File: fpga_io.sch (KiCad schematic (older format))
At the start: 27 parts, among them P1 CONN_5X2, P10 CONN_5X2, P11 CONN_5X2, P12 CONN_5X2, P13 CONN_5X2, P14 CONN_5X2, P2 CONN_5X2, P3 CONN_5X2, P4 CONN_5X2, P5 CONN_5X2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

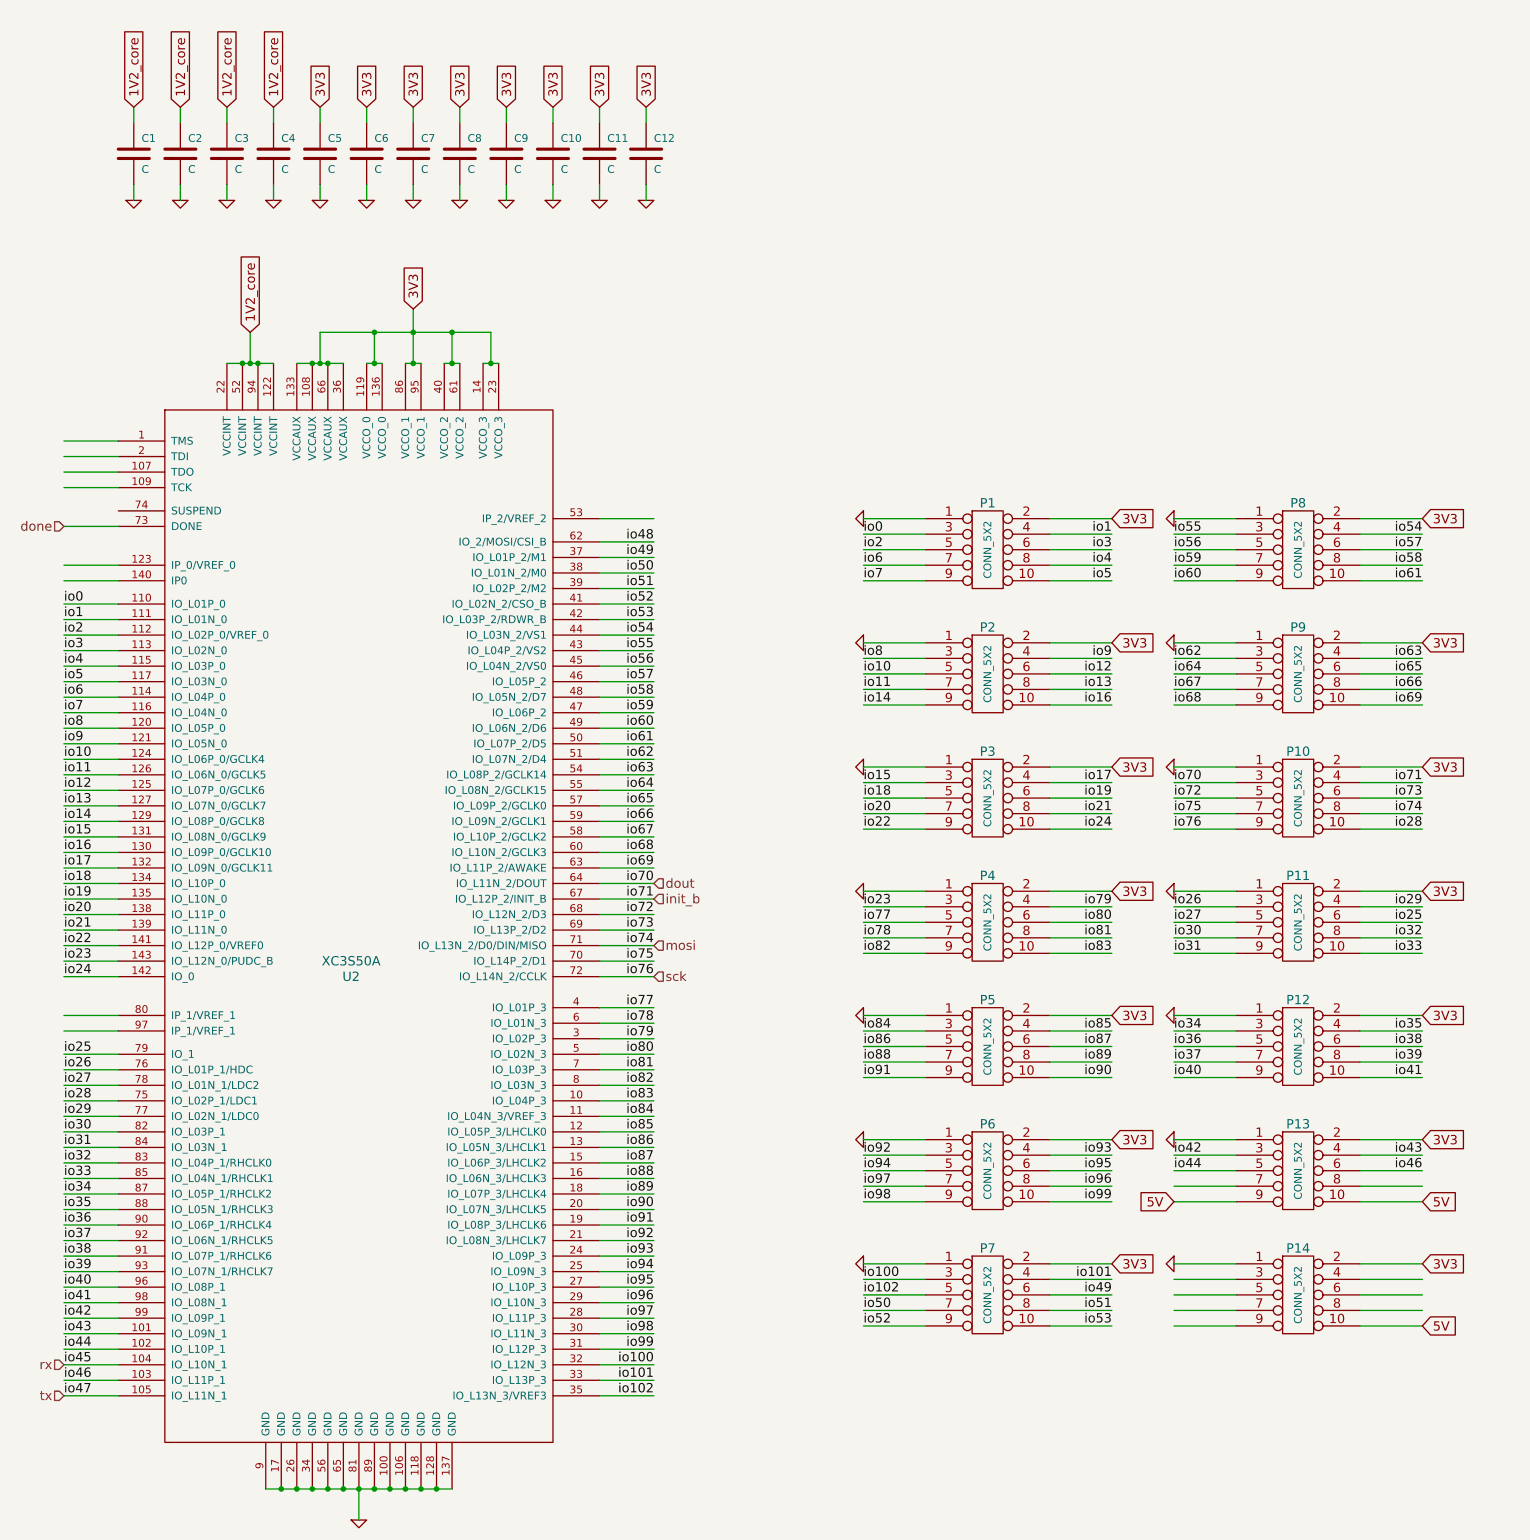
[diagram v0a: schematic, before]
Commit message: Fixed the FPGAs decoupling & power supply. Started work towards output driver modules (to be connected via 10 pin cable).
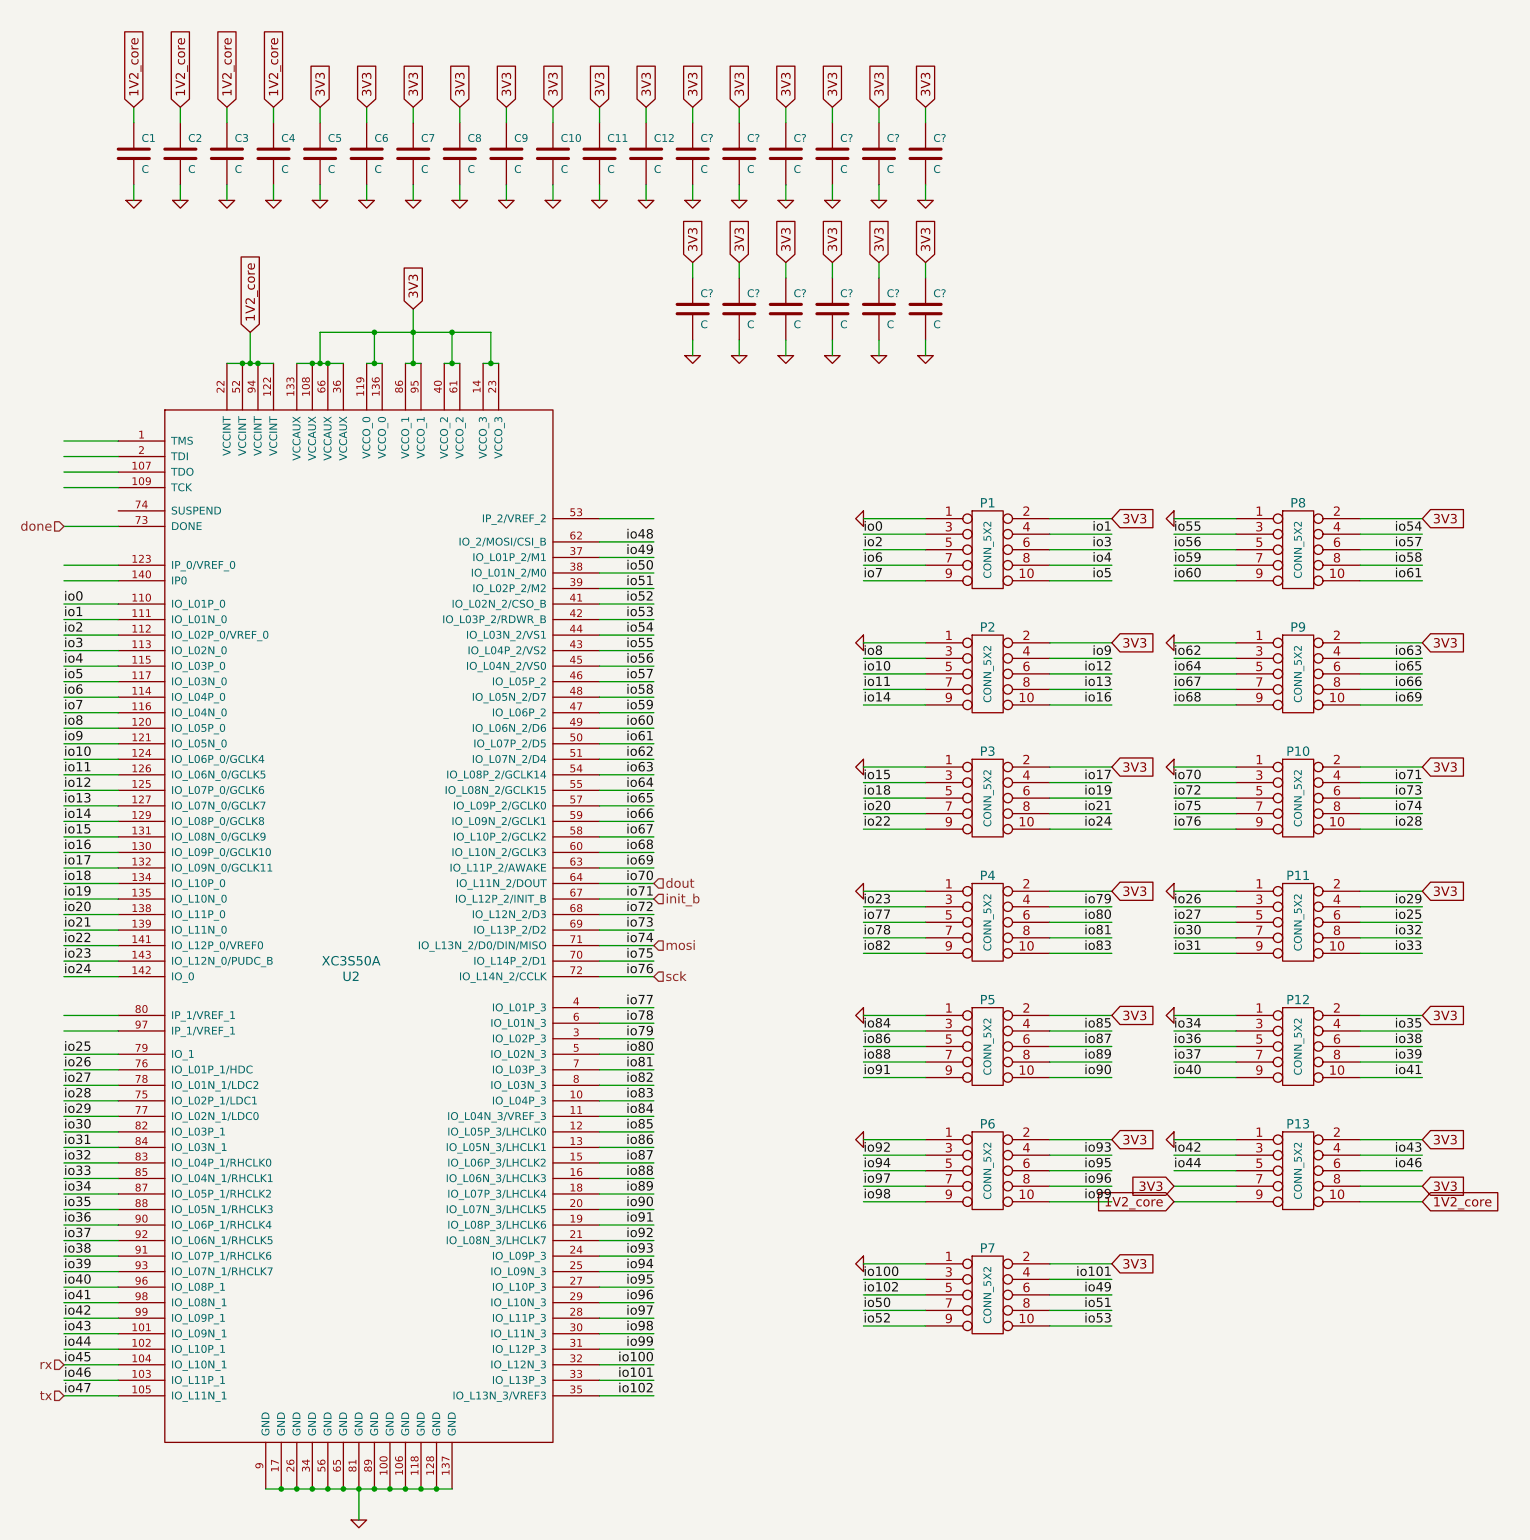
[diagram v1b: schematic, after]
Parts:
- removed P14: CONN_5X2, symbol CONN_5X2
- added C? (x12): C, symbol C
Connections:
- net labels removed: 5V
- wire segments 292 -> 306
